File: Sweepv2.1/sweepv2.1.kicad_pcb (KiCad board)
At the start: 2 copper layers, 216.9 x 86.9 mm, 51 parts, among them J1 AudioJack4dpb, J2 AudioJack4dpb, SW10 SW_Push, SW11 SW_Push, SW11_r1 SW_Push, SW12 SW_Push, SW12_r1 SW_Push, SW13_r1 SW_Push, SW14 SW_Push, SW15 SW_Push, SW15_r1 SW_Push, SW16 SW_Push, SW16_r1 SW_Push, SW17 SW_Push, SW17_r1 SW_Push, SW18 SW_Push, SW18_r1 SW_Push, SW2 SW_Push, SW20 SW_Push, SW20_r1 SW_Push, SW21 SW_Push, SW21_r1 SW_Push, SW2_r1 SW_Push, SW3 SW_Push, SW3_r1 SW_Push, SW4 SW_Push, SW4_r1 SW_Push, SW5 SW_Push, SW5_r1 SW_Push, SW6 SW_Push, SW6_r1 SW_Push, SW7_r1 SW_Push, SW8 SW_Push, SW8_r1 SW_Push, SW9 SW_Push, SW9_r1 SW_Push, U1 ProMicro-kbd, U2 ProMicro-kbd

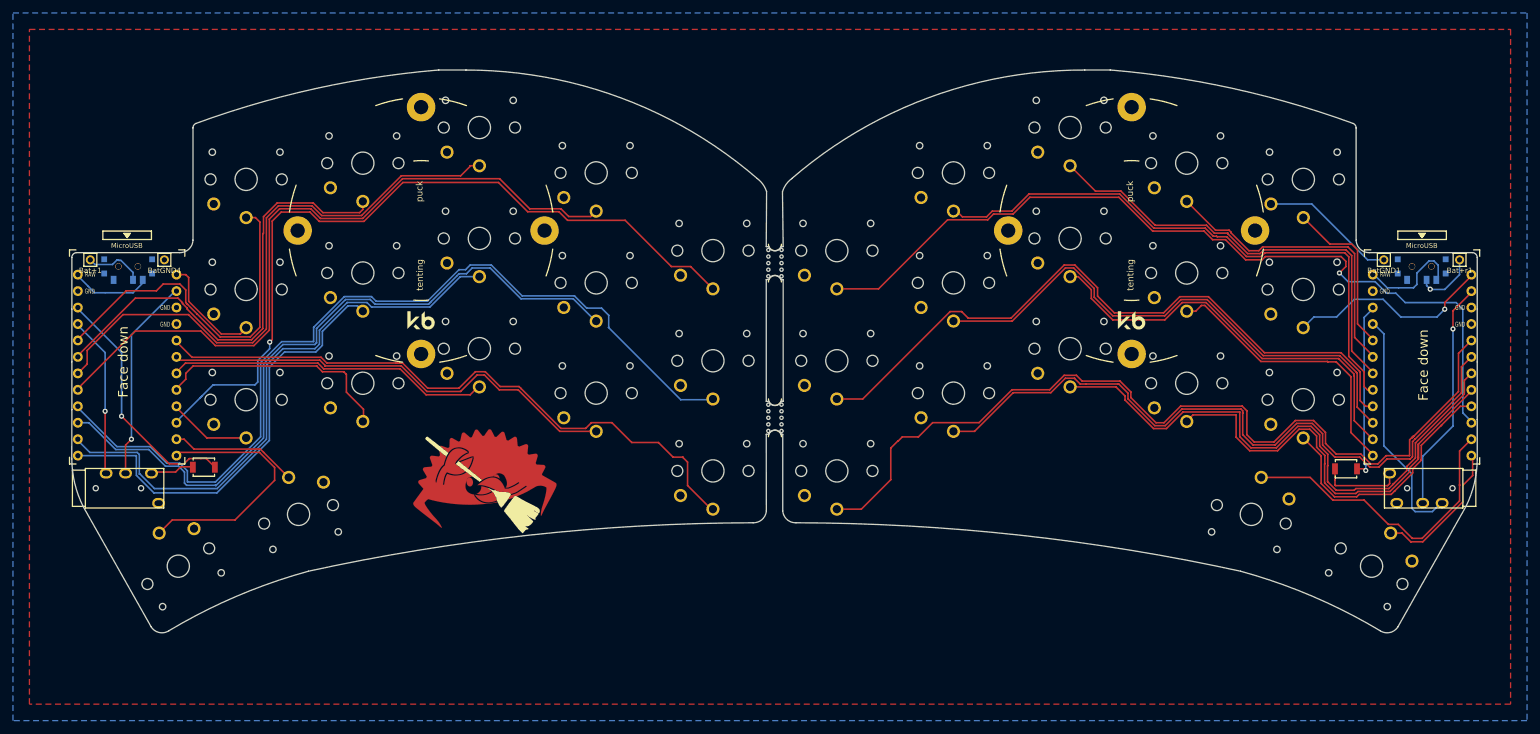
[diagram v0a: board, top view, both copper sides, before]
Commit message: PCB modifications
-Relocated TRRS port
-New PCB cutout
-Removed reset button
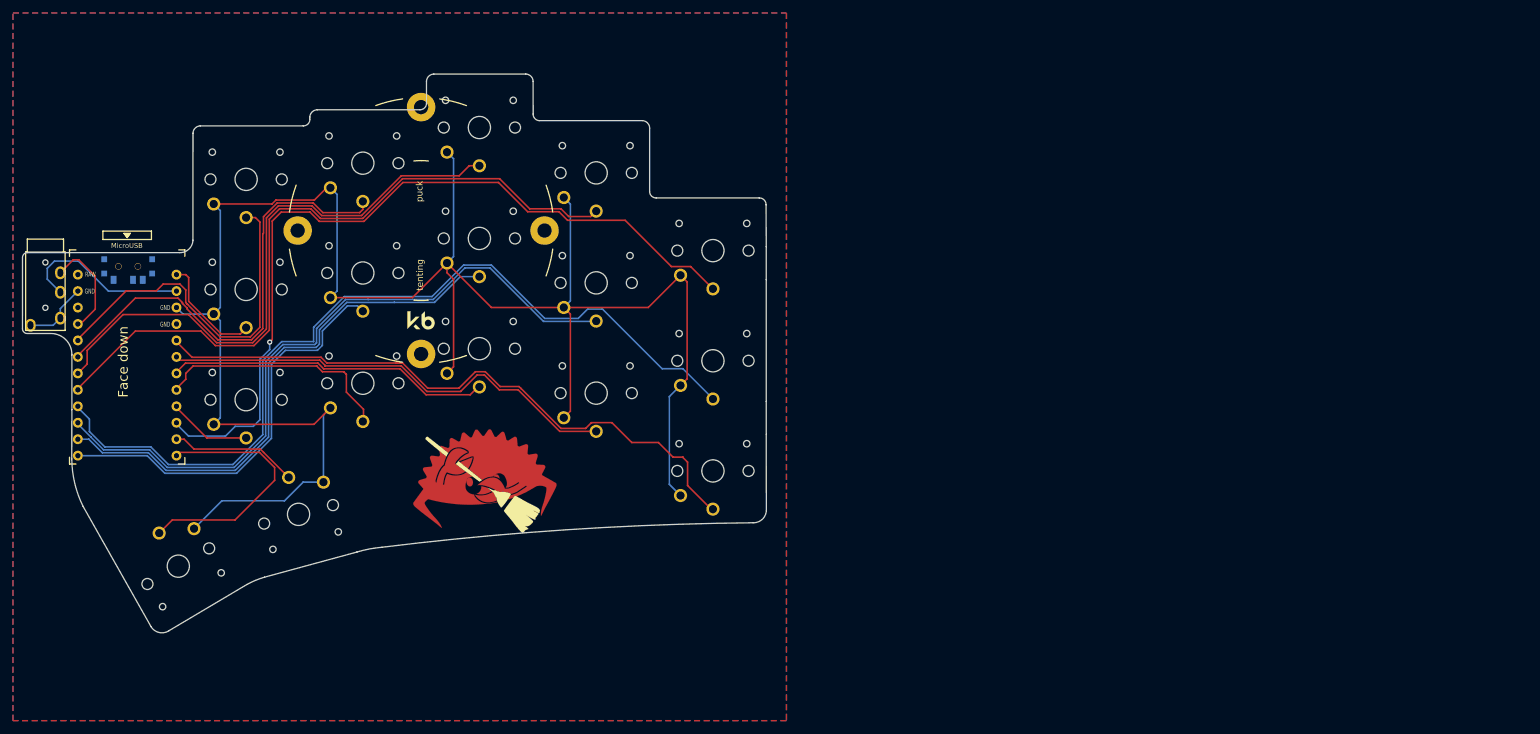
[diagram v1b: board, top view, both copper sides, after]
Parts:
- removed Bat+1, Bat+r1, BatGND1, BatGND4: MountingHole_Pad, kbd:1pin_conn
- removed J2: AudioJack4dpb, Kailh:TRRS-PJ-320A
- removed the REF** at (185.4, 46.3)
- removed RSW1, RSW2: SW_Push, kbd:SW_SPST_B3U-1000P
- removed SW10, SW11, SW12, SW14, SW15, SW16, SW17, SW18, SW2, SW20, SW21, SW3, SW4, SW5, SW6, SW8, SW9: SW_Push, Kailh:SW_PG1350_nonrev_DPB
- removed SW_POWERR1: SW_SPDT, Kailh:SPDT_C128955
- removed U1: ProMicro-kbd, kbd:ProMicro_v3_min
- removed mouse-bite-2mm-slot (x2): VAL**, Duckyb-Parts:mouse-bite-5mm-slot-with-space-for-track
- moved J1 37.0 mm to (17.7, 49.6), turned to 0 degrees
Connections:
- U2 pad 24: raw -> (no net)
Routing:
- net gnd: track 40.7 -> 311.9 mm
- net Switch11: track 136.7 -> 0.00 mm
- net Switch1: track 131.1 -> 0.00 mm, vias 1 -> 0
- net Switch12: track 108.4 -> 0.00 mm
- net Switch6: track 106.6 -> 0.00 mm
- net Switch13: track 90.5 -> 0.00 mm
- net Switch2: track 89.9 -> 0.00 mm
- net Switch7: track 83.9 -> 0.00 mm
- net Switch3: track 69.4 -> 0.00 mm
- net Switch14: track 68.6 -> 0.00 mm
- net Switch8: track 64.4 -> 0.00 mm
- net Switch16: track 47.3 -> 0.00 mm
- net Switch4: track 47.0 -> 0.00 mm
- net vcc: track 61.4 -> 16.0 mm, vias 1 -> 0
- net Switch9: track 44.0 -> 0.00 mm
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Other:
- board size 216.9 x 86.9 mm -> 114.8 x 86.2 mm
- net class Default removed
- board text removed: "Sweep is based on the Ferris."
- board text removed: "Sweep v 2.1"

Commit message: removed excess projects
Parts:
- removed G***: LOGO, Kailh:ferris_broom
- removed the REF** at (75.7, 46.3)
- removed SW_POWER1: SW_SPDT, Kailh:SPDT_C128955
- removed U2: ProMicro-kbd, kbd:ProMicro_v3_min
- added REF**: Tenting Puck, Button_Switch_Keyboard:Tenting_Puck2, F.Cu at (75.7, 52.2)
- added U1: Elite-C-29pin-holes, Button_Switch_Keyboard:Elite-C-29pin-holes, F.Cu at (30.4, 67.0)
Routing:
- net Switch6_r: track 133.7 -> 104.0 mm
- net Switch7_r: track 107.1 -> 80.2 mm
- net Switch8_r: track 84.7 -> 60.0 mm
- net Switch18_r: track 26.8 -> 2.80 mm
- net Switch5_r: track 55.7 -> 32.3 mm
- net Switch9_r: track 64.4 -> 41.7 mm
- net Switch4_r: track 71.6 -> 50.7 mm
- net Switch13_r: track 50.3 -> 70.4 mm, vias 0 -> 1
- net Switch12_r: track 71.8 -> 90.9 mm, vias 0 -> 1
- net Switch3_r: track 91.4 -> 72.4 mm
- net Switch11_r: track 99.8 -> 117.8 mm, vias 0 -> 1
- net Switch14_r: track 37.6 -> 55.1 mm, vias 0 -> 1
- net Switch17_r: track 39.7 -> 22.7 mm
- net Switch10_r: track 17.2 -> 33.9 mm
- net Switch2_r: track 109.6 -> 94.5 mm
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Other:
- outline, holes or cut-outs redrawn
- board text added: "Chipside Up"
- board text removed: "Face down"
